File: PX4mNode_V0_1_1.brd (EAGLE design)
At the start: 48.6 x 34.9 mm, 135 parts, among them J201 DF13C-6P-1.25V, J202 DF13C-6P-1.25V, J203 DF13C-6P-1.25V, J301 DF13C-4P-1.25V, J401 DF13C-7P-1.25V, J402 DF13-4P-1.25V, J403 DF13C-4P-1.25V, J404 DF13C-4P-1.25V, J405 DF13C-4P-1.25V, J801 DF13C-3P-1.25V, M3_MOUNT1101 MOUNT-HOLE3.1MM, M3_MOUNT1102 MOUNT-HOLE3.1MM, M3_MOUNT1103 MOUNT-HOLE3.1MM, M3_MOUNT1104 MOUNT-HOLE3.1MM, U101 STM32F4X7VX, U401 MAX3051, U402 MAX3051, X101 3.2x2.5 mm / 24 MHz / 15 ppm

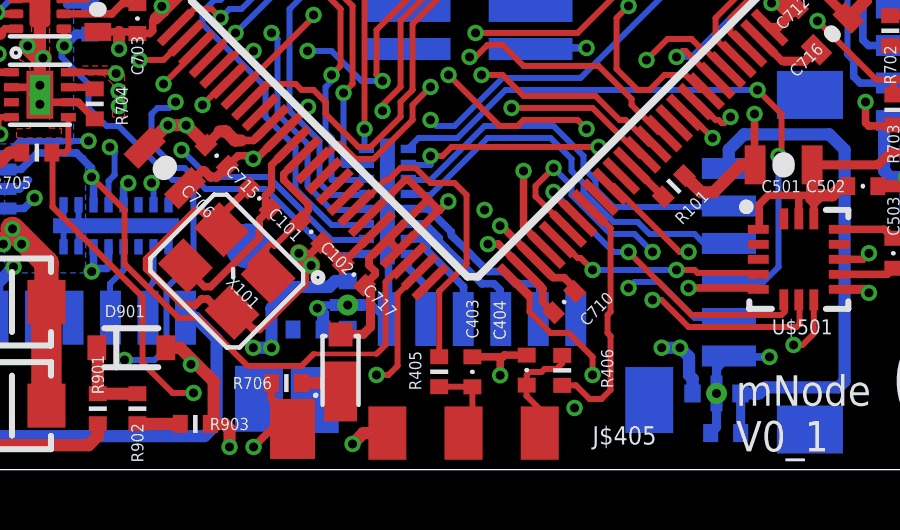
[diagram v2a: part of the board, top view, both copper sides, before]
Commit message: Reconnected missing UART filtered 5V power
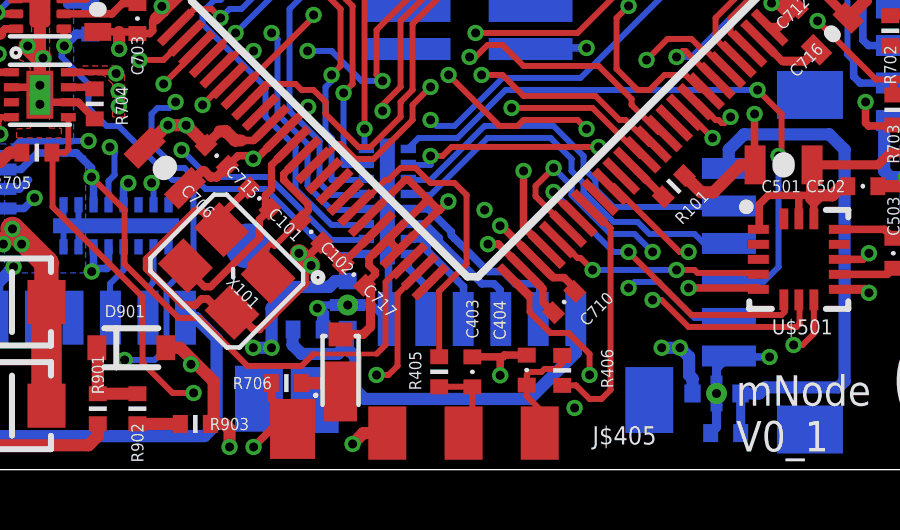
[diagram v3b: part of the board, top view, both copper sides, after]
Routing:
- net 5V_S2_FILTERED: track 0.00 -> 14.5 mm
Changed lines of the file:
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@@
 <grid distance="0.1" unitdist="mm" unit="mm" style="dots" multiple="1" display="yes" altdistance="4" altunitdist="mil" altunit="mm"/>
 <layers>
-<layer number="1" name="Top" color="4" fill="1" visible="yes" active="yes"/>
+<layer number="1" name="Top" color="4" fill="1" visible="no" active="yes"/>
 <layer number="2" name="Ground" color="2" fill="10" visible="no" active="yes"/>
-<layer number="3" name="Horizontal" color="13" fill="15" visible="yes" active="yes"/>
+<layer number="3" name="Horizontal" color="13" fill="15" visible="no" active="yes"/>
 <layer number="4" name="Route4" color="1" fill="4" visible="no" active="no"/>
 <layer number="5" name="Route5" color="4" fill="4" visible="no" active="no"/>
@@
 <layer number="12" name="Route12" color="1" fill="5" visible="no" active="no"/>
 <layer number="13" name="Route13" color="4" fill="5" visible="no" active="no"/>
-<layer number="14" name="Vertical" color="14" fill="15" visible="yes" active="yes"/>
-<layer number="15" name="Power" color="11" fill="15" visible="yes" active="yes"/>
+<layer number="14" name="Vertical" color="14" fill="15" visible="no" active="yes"/>
+<layer number="15" name="Power" color="11" fill="15" visible="no" active="yes"/>
 <layer number="16" name="Bottom" color="1" fill="1" visible="yes" active="yes"/>
 <layer number="17" name="Pads" color="2" fill="1" visible="yes" active="yes"/>
@@
 <layer number="19" name="Unrouted" color="14" fill="1" visible="yes" active="yes"/>
 <layer number="20" name="Dimension" color="15" fill="1" visible="yes" active="yes"/>
-<layer number="21" name="tPlace" color="7" fill="1" visible="yes" active="yes"/>
+<layer number="21" name="tPlace" color="7" fill="1" visible="no" active="yes"/>
 <layer number="22" name="bPlace" color="7" fill="1" visible="yes" active="yes"/>
-<layer number="23" name="tOrigins" color="15" fill="1" visible="yes" active="yes"/>
+<layer number="23" name="tOrigins" color="15" fill="1" visible="no" active="yes"/>
 <layer number="24" name="bOrigins" color="15" fill="1" visible="yes" active="yes"/>
 <layer number="25" name="tNames" color="7" fill="1" visible="no" active="yes"/>
@@
 <layer number="37" name="tTest" color="7" fill="1" visible="no" active="yes"/>
 <layer number="38" name="bTest" color="7" fill="1" visible="no" active="yes"/>
-<layer number="39" name="tKeepout" color="4" fill="11" visible="yes" active="yes"/>
+<layer number="39" name="tKeepout" color="4" fill="11" visible="no" active="yes"/>
 <layer number="40" name="bKeepout" color="1" fill="11" visible="yes" active="yes"/>
-<layer number="41" name="tRestrict" color="4" fill="10" visible="yes" active="yes"/>
+<layer number="41" name="tRestrict" color="4" fill="10" visible="no" active="yes"/>
 <layer number="42" name="bRestrict" color="1" fill="10" visible="yes" active="yes"/>
 <layer number="43" name="vRestrict" color="2" fill="10" visible="no" active="yes"/>
@@
 <layer number="49" name="Reference" color="7" fill="1" visible="no" active="yes"/>
 <layer number="50" name="dxf" color="7" fill="1" visible="no" active="yes"/>
-<layer number="51" name="tDocu" color="7" fill="1" visible="yes" active="yes"/>
+<layer number="51" name="tDocu" color="7" fill="1" visible="no" active="yes"/>
 <layer number="52" name="bDocu" color="7" fill="1" visible="yes" active="yes"/>
 <layer number="53" name="tGND_GNDA" color="7" fill="9" visible="no" active="no"/>
@@
 <wire x1="35" y1="7.5" x2="34.75" y2="7.25" width="0.3048" layer="1"/>
 <wire x1="34.75" y1="7.25" x2="34" y2="7.25" width="0.3048" layer="1"/>
-<wire x1="48.7" y1="26.8" x2="49.2888" y2="26.8208" width="0" layer="19" extent="1-1"/>
-<wire x1="48.6664" y1="18.6944" x2="50.892" y2="21.2344" width="0" layer="19" extent="1-15"/>
-<wire x1="48.9" y1="18" x2="49.22724375" y2="18.13764375" width="0" layer="19" extent="1-1"/>
-<wire x1="49.1504" y1="17.3496" x2="48.572984375" y2="17.483384375" width="0" layer="19" extent="1-15"/>
-<wire x1="42.2" y1="21.8" x2="48.3616" y2="18.6944" width="0" layer="19" extent="1-15"/>
-<wire x1="38.9" y1="28.1" x2="40.3352" y2="21.844" width="0" layer="19" extent="1-16"/>
-<wire x1="38.4016" y1="28.0832" x2="38.4" y2="28.1" width="0" layer="19" extent="1-1"/>
-<wire x1="29.2916" y1="28.332" x2="35.1536" y2="30.988" width="0" layer="19" extent="1-16"/>
-<wire x1="21.8" y1="10.4" x2="21.8" y2="10.9" width="0" layer="19" extent="16-16"/>
-<wire x1="30.5816" y1="13.208" x2="28.0416" y2="18.8976" width="0" layer="19" extent="1-1"/>
-<wire x1="34.869265625" y1="11.119425" x2="32.0408375" y2="13.94785" width="0" layer="19" extent="1-1"/>
-<wire x1="39.3192" y1="10.8712" x2="37.592" y2="11.684" width="0" layer="19" extent="1-1"/>
+<wire x1="21.8" y1="10.9" x2="21.8" y2="10.4" width="0" layer="19" extent="16-16"/>
 </signal>
 <signal name="OTG_FS_DP">
@@
 <contactref element="U101" pad="33"/>
 <contactref element="R406" pad="P$1"/>
-<wire x1="43" y1="10.8" x2="43" y2="8" width="0.2" layer="1"/>
-<wire x1="43" y1="8" x2="42.9" y2="7.9" width="0.2" layer="1"/>
-<wire x1="42.9" y1="7.9" x2="42.9" y2="7.3" width="0.2" layer="1"/>
-<wire x1="42.9" y1="7.3" x2="43" y2="7.2" width="0.2" layer="1"/>
-<wire x1="43" y1="7.2" x2="43" y2="5.4" width="0.2" layer="1"/>
+<wire x1="43" y1="10.8" x2="43" y2="5.4" width="0.2" layer="1"/>
 <wire x1="42.3" y1="11.5" x2="43" y2="10.8" width="0.2" layer="1"/>
 <wire x1="42.3" y1="11.5" x2="42.293884375" y2="11.472978125" width="0.2" layer="1"/>
@@
 <contactref element="L204" pad="P$2"/>
 <contactref element="U$203" pad="C"/>
-<wire x1="34.2392" y1="7.4296" x2="41.841" y2="7.764" width="0" layer="19" extent="16-16"/>
-<wire x1="32.4184" y1="7.4168" x2="34.2392" y2="7.4296" width="0" layer="19" extent="16-16"/>
+<wire x1="32.4184" y1="7.4168" x2="32.4" y2="7.4168" width="0.4064" layer="16"/>
+<wire x1="32.4" y1="7.4168" x2="32.4" y2="6.9" width="0.4064" layer="16"/>
+<wire x1="32.4" y1="6.9" x2="32.7" y2="6.6" width="0.4064" layer="16"/>
+<wire x1="32.7" y1="6.6" x2="33.9" y2="6.6" width="0.4064" layer="16"/>
+<wire x1="33.9" y1="6.6" x2="34.2392" y2="6.9392" width="0.4064" layer="16"/>
+<wire x1="34.2392" y1="6.9392" x2="34.2392" y2="7.4296" width="0.4064" layer="16"/>
+<wire x1="34.2392" y1="7.4296" x2="34.2392" y2="6.7608" width="0.4064" layer="16"/>
+<wire x1="34.2392" y1="6.7608" x2="34.5" y2="6.5" width="0.4064" layer="16"/>
+<wire x1="34.5" y1="6.5" x2="34.5" y2="5.4" width="0.4064" layer="16"/>
+<wire x1="34.5" y1="5.4" x2="34.8" y2="5.1" width="0.4064" layer="16"/>
+<wire x1="34.8" y1="5.1" x2="40.3" y2="5.1" width="0.4064" layer="16"/>
+<wire x1="40.3" y1="5.1" x2="41.841" y2="6.641" width="0.4064" layer="16"/>
+<wire x1="41.841" y1="6.641" x2="41.841" y2="7.764" width="0.4064" layer="16"/>
 </signal>
 <signal name="FMU-!RESET">
@@
 <wire x1="25.1872" y1="17.2624" x2="24.7904" y2="16.8656" width="0.3048" layer="16"/>
 <contactref element="U101" pad="26"/>
-<wire x1="42.4" y1="6.5" x2="42.4" y2="5.9" width="0.2" layer="1"/>
-<wire x1="41.6" y1="7.3" x2="42.4" y2="6.5" width="0.2" layer="1"/>
+<wire x1="42.3" y1="6.6" x2="42.3" y2="5.9" width="0.2" layer="1"/>
+<wire x1="41.6" y1="7.3" x2="42.3" y2="6.6" width="0.2" layer="1"/>
 <wire x1="41" y1="7.3" x2="41.6" y2="7.3" width="0.2" layer="1"/>
 <wire x1="40.3" y1="8" x2="41" y2="7.3" width="0.2" layer="1"/>
@@
 <wire x1="39.9" y1="9" x2="40.3" y2="8.6" width="0.2" layer="1"/>
 <wire x1="39.9" y1="9" x2="39.8190125" y2="8.998103125" width="0.2" layer="1"/>
-<via x="42.4" y="5.9" extent="1-16" drill="0.3"/>
+<via x="42.3" y="5.9" extent="1-16" drill="0.3"/>
 <wire x1="26.2" y1="14.2" x2="25.6" y2="14.8" width="0.2" layer="16"/>
 <wire x1="26.6" y1="14.2" x2="26.2" y2="14.2" width="0.2" layer="16"/>
@@
 <wire x1="39.6" y1="5.4" x2="42" y2="5.4" width="0.2" layer="15"/>
 <wire x1="39.5" y1="5.3" x2="39.6" y2="5.4" width="0.2" layer="15"/>
-<wire x1="42.4" y1="5.8" x2="42" y2="5.4" width="0.2" layer="15"/>
-<wire x1="42.4" y1="5.9" x2="42.4" y2="5.8" width="0.2" layer="15"/>
+<wire x1="42.3" y1="5.7" x2="42" y2="5.4" width="0.2" layer="15"/>
+<wire x1="42.3" y1="5.9" x2="42.3" y2="5.7" width="0.2" layer="15"/>
 </signal>
 <signal name="VBUS" class="1">

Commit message: tweaks
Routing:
- net GND: vias 60 -> 61
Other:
- board text added: "CH1"
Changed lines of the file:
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@@
 <layer number="17" name="Pads" color="2" fill="1" visible="yes" active="yes"/>
 <layer number="18" name="Vias" color="2" fill="1" visible="yes" active="yes"/>
-<layer number="19" name="Unrouted" color="14" fill="1" visible="yes" active="yes"/>
+<layer number="19" name="Unrouted" color="14" fill="1" visible="no" active="yes"/>
 <layer number="20" name="Dimension" color="15" fill="1" visible="yes" active="yes"/>
 <layer number="21" name="tPlace" color="7" fill="1" visible="no" active="yes"/>
@@
 <text x="19.1112" y="17.0632" size="0.762" layer="22" font="vector" ratio="15" rot="MR180">5V</text>
 <text x="40.8504" y="32.1848" size="0.8128" layer="21" font="vector" ratio="15" rot="R90">CANpwr</text>
+<text x="14.5896" y="33.0056" size="1.016" layer="22" font="vector" ratio="15" rot="MR180">CH1</text>
 </plain>
 <attributes>
@@
 <wire x1="27.4" y1="6.3" x2="28.4" y2="5.3" width="0.2" layer="1"/>
 <wire x1="27.4" y1="8.5" x2="27.4" y2="6.3" width="0.2" layer="1"/>
-<wire x1="24.4" y1="11.5" x2="27.4" y2="8.5" width="0.2" layer="1"/>
-<wire x1="24.4" y1="13.3" x2="24.4" y2="11.5" width="0.2" layer="1"/>
+<wire x1="26.1" y1="9.8" x2="27.4" y2="8.5" width="0.2" layer="1"/>
 <wire x1="42.6" y1="25.9" x2="42.647440625" y2="25.968665625" width="0.2" layer="1"/>
 <wire x1="24.4" y1="13.3" x2="24.376" y2="13.3112" width="0.2" layer="1"/>
@@
 <via x="29.1" y="5.3" extent="1-16" drill="0.3" diameter="0.55"/>
 <wire x1="24.376" y1="13.3112" x2="24.8112" y2="13.3112" width="0.2" layer="1"/>
-<wire x1="24.8112" y1="13.3112" x2="24.9276" y2="13.4276" width="0.2" layer="1"/>
+<wire x1="24.8112" y1="13.3112" x2="24.9" y2="13.4" width="0.2" layer="1"/>
+<wire x1="24.9" y1="13.4" x2="24.9276" y2="13.4276" width="0.2" layer="1"/>
 <wire x1="24.9276" y1="13.4276" x2="24.9276" y2="14.49" width="0.2" layer="1"/>
 <wire x1="29.1" y1="5.3" x2="33.2" y2="5.3" width="0.254" layer="3"/>
 <wire x1="33.2" y1="5.3" x2="33.7" y2="4.8" width="0.254" layer="3"/>
 <wire x1="33.7" y1="4.8" x2="41.8" y2="4.8" width="0.254" layer="3"/>
+<wire x1="26.1" y1="9.8" x2="26.1" y2="11.2" width="0.2" layer="1"/>
+<wire x1="26.1" y1="11.2" x2="25" y2="12.3" width="0.2" layer="1"/>
+<wire x1="25" y1="12.3" x2="25" y2="13.3" width="0.2" layer="1"/>
+<wire x1="25" y1="13.3" x2="24.9" y2="13.4" width="0.2" layer="1"/>
 </signal>
 <signal name="N$8">
@@
 <wire x1="38.4" y1="32.6786" x2="38.4" y2="32.7" width="0.4064" layer="16"/>
 <wire x1="38.4" y1="32.7" x2="38.3" y2="32.8" width="0.4064" layer="16"/>
+<via x="24.3" y="12.3" extent="1-16" drill="0.3"/>
 <wire x1="46.228" y1="27.1272" x2="46.228" y2="27.5272" width="0" layer="19" extent="16-16"/>
 </signal>
@@
 <wire x1="46.5328" y1="6.8072" x2="45.3136" y2="6.8072" width="0.8128" layer="15"/>
 <wire x1="27.2872" y1="7.9248" x2="27.2872" y2="10.768" width="0.8128" layer="15"/>
-<wire x1="27.2872" y1="10.768" x2="24.668" y2="10.8872" width="0.8128" layer="15"/>
-<wire x1="24.668" y1="10.8872" x2="24.668" y2="12.5048" width="0.8128" layer="15"/>
-<wire x1="24.668" y1="12.5048" x2="24.6808" y2="13.3176" width="0.8128" layer="15"/>
+<wire x1="27.2872" y1="10.768" x2="24.968" y2="10.7872" width="0.8128" layer="15"/>
+<wire x1="24.968" y1="10.7872" x2="24.968" y2="11.7048" width="0.8128" layer="15"/>
+<wire x1="24.968" y1="11.7048" x2="25" y2="12.8" width="0.4064" layer="15"/>
+<wire x1="25" y1="12.8" x2="24.6808" y2="13.1192" width="0.4064" layer="15"/>
+<wire x1="24.6808" y1="13.1192" x2="24.6808" y2="13.3176" width="0.4064" layer="15"/>
 <wire x1="24.6808" y1="13.3176" x2="24.7" y2="14.0176" width="0.8128" layer="15"/>
 <via x="31.6992" y="6.8072" extent="1-16" drill="0.3" diameter="0.55"/>
@@
 <polygon width="0.2" layer="15" thermals="no">
 <vertex x="12.5936" y="31.7024"/>
-<vertex x="14.2336" y="31.7024"/>
+<vertex x="14.3336" y="31.7024"/>
 <vertex x="14.3336" y="12.4"/>
 <vertex x="13.2224" y="12.3888"/>

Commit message: Graphic shuffle
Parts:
- moved OSHW_LOGO 0.61 mm to (50.8, 35.5)
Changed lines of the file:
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@@
 <layer number="17" name="Pads" color="2" fill="1" visible="yes" active="yes"/>
 <layer number="18" name="Vias" color="2" fill="1" visible="yes" active="yes"/>
-<layer number="19" name="Unrouted" color="14" fill="1" visible="no" active="yes"/>
+<layer number="19" name="Unrouted" color="14" fill="1" visible="yes" active="yes"/>
 <layer number="20" name="Dimension" color="15" fill="1" visible="yes" active="yes"/>
 <layer number="21" name="tPlace" color="7" fill="1" visible="no" active="yes"/>
@@
 <attribute name="PARTNO" value="DF13C-6P-1.25V(20)" x="38.716" y="6.864" size="1.778" layer="28" rot="MR0" display="off"/>
 </element>
-<element name="OSHW_LOGO" library="pixhawk2" package="OSHW-LOGO-S" value="OSHW-LOGOS" x="50.2312" y="35.352">
-<attribute name="PARTNO" value="*" x="50.2312" y="46.528" size="1.778" layer="27" display="off"/>
-<attribute name="BOM" value="EXCLUDE" x="50.2312" y="46.528" size="1.778" layer="27" display="off"/>
+<element name="OSHW_LOGO" library="pixhawk2" package="OSHW-LOGO-S" value="OSHW-LOGOS" x="50.8312" y="35.452">
+<attribute name="PARTNO" value="*" x="50.8312" y="46.628" size="1.778" layer="27" display="off"/>
+<attribute name="BOM" value="EXCLUDE" x="50.8312" y="46.628" size="1.778" layer="27" display="off"/>
 </element>
 <element name="M3_MOUNT1104" library="pixhawk2" package="MOUNT-HOLE3.1" value="MOUNT-HOLE3.1MM" x="12.2" y="5.7" locked="yes">

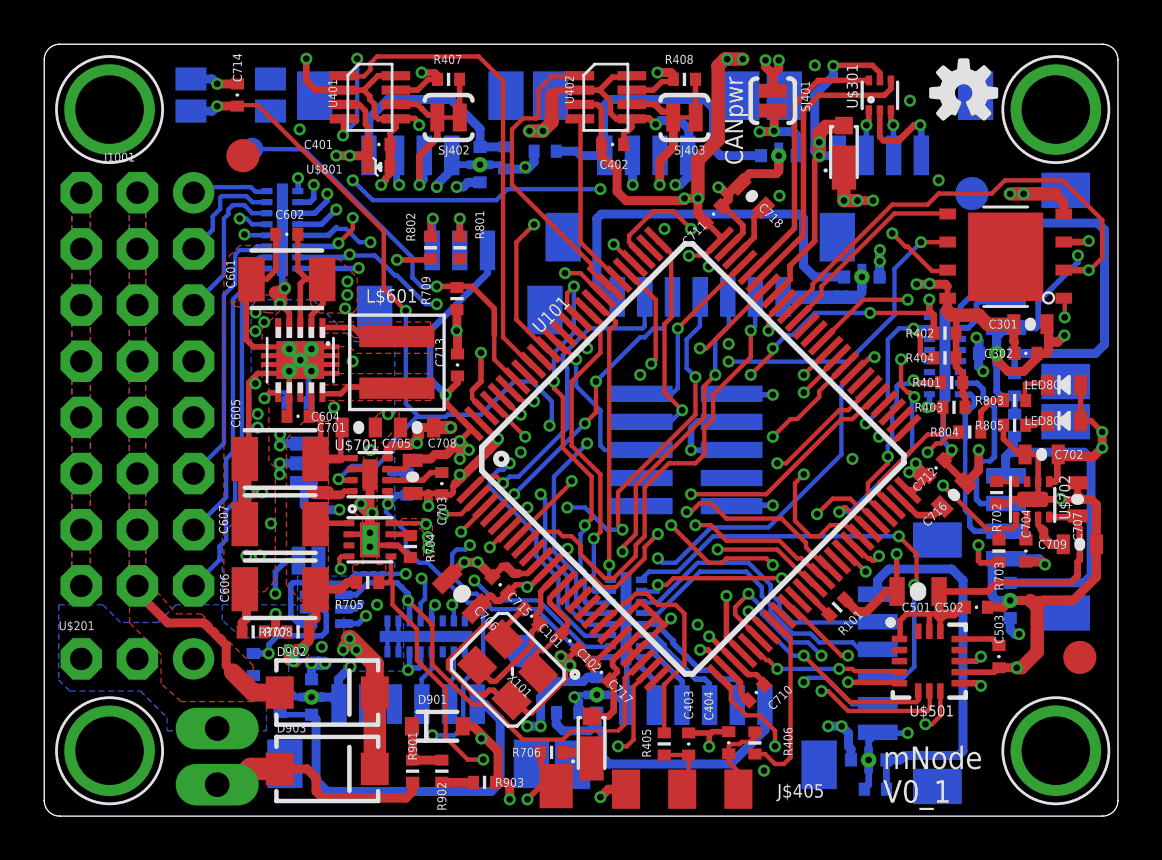
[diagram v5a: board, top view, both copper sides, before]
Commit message: Realigned bad autoroute alignment on microcontroller pins
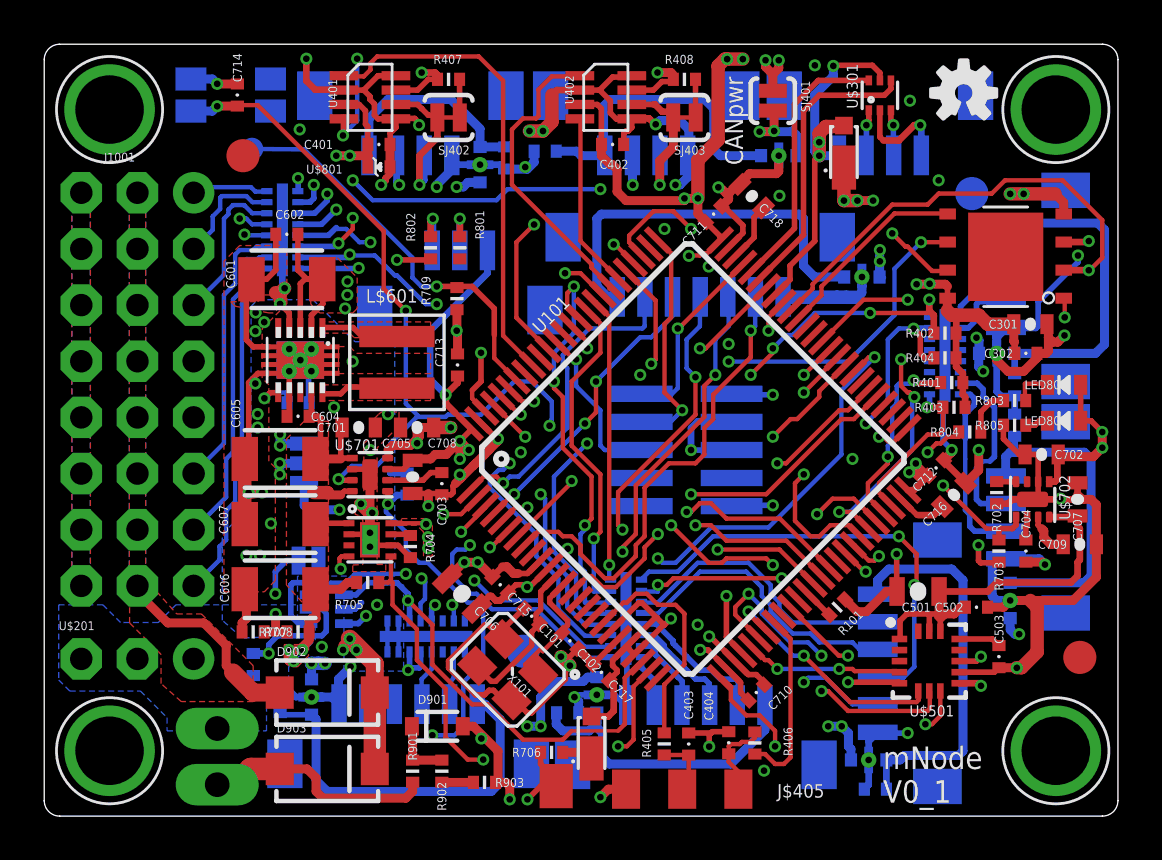
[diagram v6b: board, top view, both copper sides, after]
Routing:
- net SPI_EXT_MOSI: vias 4 -> 3
